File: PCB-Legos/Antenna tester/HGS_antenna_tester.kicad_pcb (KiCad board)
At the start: 4 copper layers, 100 x 100 mm, 10 parts, among them J1 Conn_Coaxial, J2 Conn_01x01

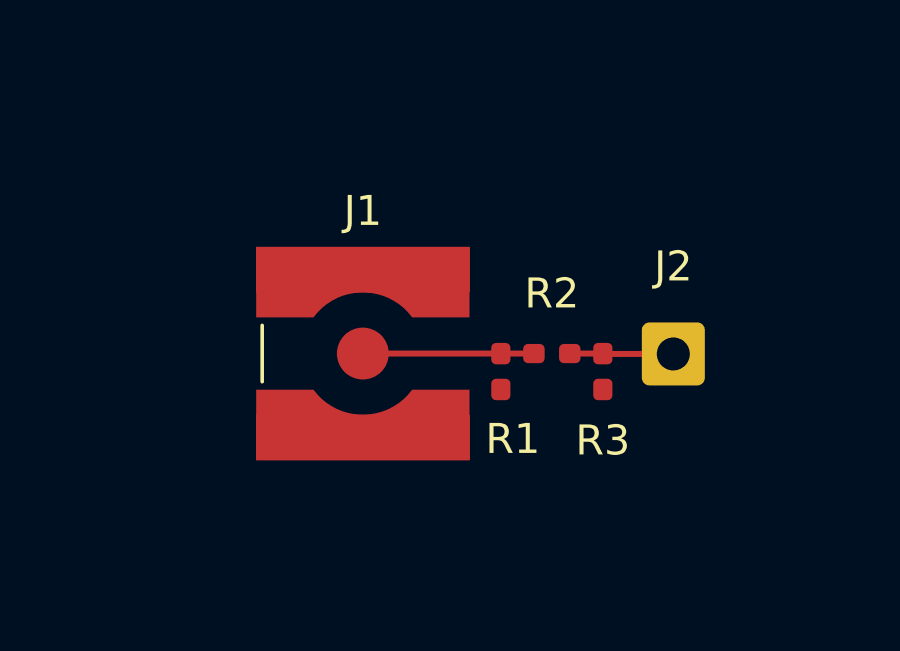
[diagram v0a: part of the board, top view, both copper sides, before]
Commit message: fixed microstrip width and moved SMA away from R1
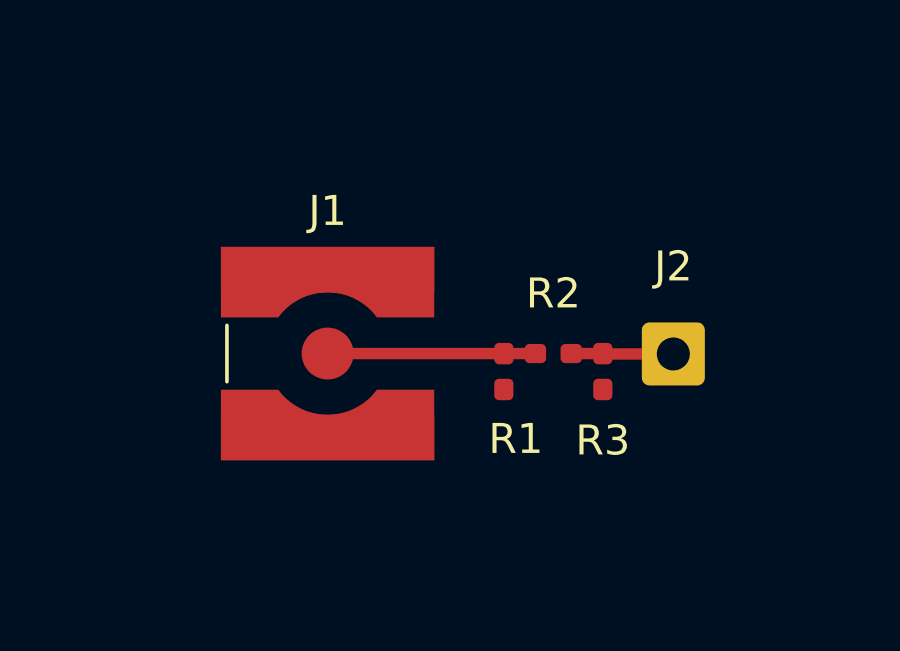
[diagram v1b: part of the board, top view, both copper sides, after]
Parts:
- moved J1 1.17 mm to (127.3, 85.0)
- moved R1 0.10 mm to (133.2, 85.6)
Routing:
- net Net-(J1-Pad1): track 5.71 -> 6.88 mm
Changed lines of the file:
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@@
     (pad "" np_thru_hole circle (at 0 0) (size 4.5 4.5) (drill 4.5) (layers *.Cu *.Mask))
   )
-  (footprint "Connector_Coaxial:SMA_Amphenol_132134-10_Vertical" locked (layer "F.Cu")
-    (at 128.5 85)
+  (footprint "Connector_Coaxial:SMA_Amphenol_132134-10_Vertical" (layer "F.Cu")
+    (at 127.325 85)
     (descr "https://www.amphenolrf.com/downloads/dl/file/id/4007/product/2974/132134_10_customer_drawing.pdf")
     (tags "SMA SMD Female Jack Vertical")
@@
     (pad "1" smd circle locked (at 0 0 90) (size 1.73 1.73) (layers "F.Cu" "F.Paste" "F.Mask")
       (net 2 "Net-(J1-Pad1)") (pinfunction "In") (pintype "passive"))
-    (pad "2" smd custom locked (at 0 2.8) (size 7.11 1.51) (layers "F.Cu" "F.Paste" "F.Mask")
+    (pad "2" smd custom (at 0 2.8) (size 7.11 1.51) (layers "F.Cu" "F.Paste" "F.Mask")
       (net 3 "GND") (pinfunction "Ext") (pintype "passive") (zone_connect 2)
       (options (clearance outline) (anchor rect))
@@
           ) (width 0) (fill yes))
       ))
-    (pad "2" smd custom locked (at 0 -2.8 180) (size 7.11 1.51) (layers "F.Cu" "F.Paste" "F.Mask")
+    (pad "2" smd custom (at 0 -2.8 180) (size 7.11 1.51) (layers "F.Cu" "F.Paste" "F.Mask")
       (net 3 "GND") (pinfunction "Ext") (pintype "passive") (zone_connect 2)
       (options (clearance outline) (anchor rect))
@@
   )
   (footprint "Resistor_SMD:R_0402_1005Metric_Pad0.72x0.64mm_HandSolder" (layer "F.Cu")
-    (at 134.8 85)
+    (at 134.85 85)
     (descr "Resistor SMD 0402 (1005 Metric), square (rectangular) end terminal, IPC_7351 nominal with elongated pad for handsoldering. (Body size source: IPC-SM-782 page 72, https://www.pcb-3d.com/wordpress/wp-content/uploads/ipc-sm-782a_amendment_1_and_2.pdf), generated with kicad-footprint-generator")
     (tags "resistor handsolder")
@@
   )
   (footprint "Resistor_SMD:R_0402_1005Metric_Pad0.72x0.64mm_HandSolder" (layer "F.Cu")
-    (at 133.1 85.6 -90)
+    (at 133.2 85.6 -90)
     (descr "Resistor SMD 0402 (1005 Metric), square (rectangular) end terminal, IPC_7351 nominal with elongated pad for handsoldering. (Body size source: IPC-SM-782 page 72, https://www.pcb-3d.com/wordpress/wp-content/uploads/ipc-sm-782a_amendment_1_and_2.pdf), generated with kicad-footprint-generator")
     (tags "resistor handsolder")
@@
   (segment (start 136.5 85.0025) (end 136.4975 85) (width 0.2) (layer "F.Cu") (net 1))
   (segment (start 136.511 85.0135) (end 136.5 85.0025) (width 0.2) (layer "F.Cu") (net 1))
-  (segment (start 138.8511 85.0135) (end 136.511 85.0135) (width 0.2) (layer "F.Cu") (net 1))
-  (segment (start 136.4975 85) (end 135.3975 85) (width 0.2) (layer "F.Cu") (net 1))
+  (segment (start 138.8511 85.0135) (end 136.511 85.0135) (width 0.38) (layer "F.Cu") (net 1))
+  (segment (start 136.4975 85) (end 135.3975 85) (width 0.38) (layer "F.Cu") (net 1))
   (segment (start 138.8401 85.0025) (end 138.8511 85.0135) (width 0.2) (layer "F.Cu") (net 1))
+  (segment (start 133.0975 85) (end 127.325 85) (width 0.38) (layer "F.Cu") (net 2))
   (segment (start 134.2 85.0025) (end 134.2025 85) (width 0.2) (layer "F.Cu") (net 2))
-  (segment (start 134.2025 85) (end 133.1025 85) (width 0.2) (layer "F.Cu") (net 2))
+  (segment (start 134.2025 85) (end 133.1025 85) (width 0.38) (layer "F.Cu") (net 2))
   (segment (start 133.1025 85) (end 133.1 85.0025) (width 0.2) (layer "F.Cu") (net 2))
   (segment (start 133.1 85.0025) (end 133.0975 85) (width 0.2) (layer "F.Cu") (net 2))
-  (segment (start 133.0975 85) (end 128.5 85) (width 0.2) (layer "F.Cu") (net 2))
   (zone (net 0) (net_name "") (layer "F.Cu") (hatch full 0.508)
     (connect_pads (clearance 0))

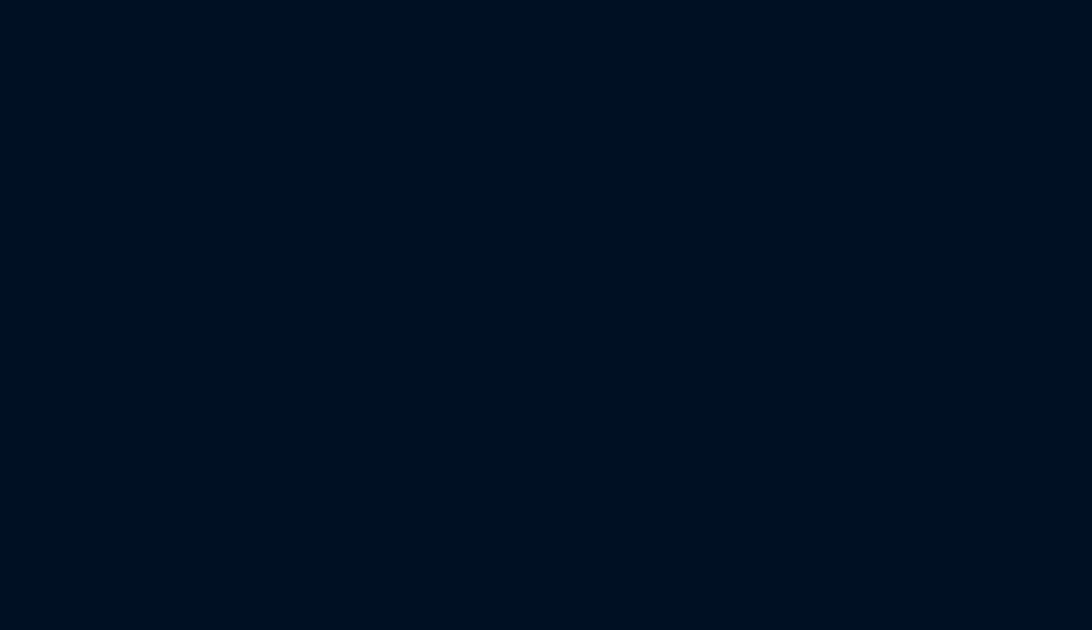
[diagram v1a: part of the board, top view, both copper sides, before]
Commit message: added missing antenna form mounting holes
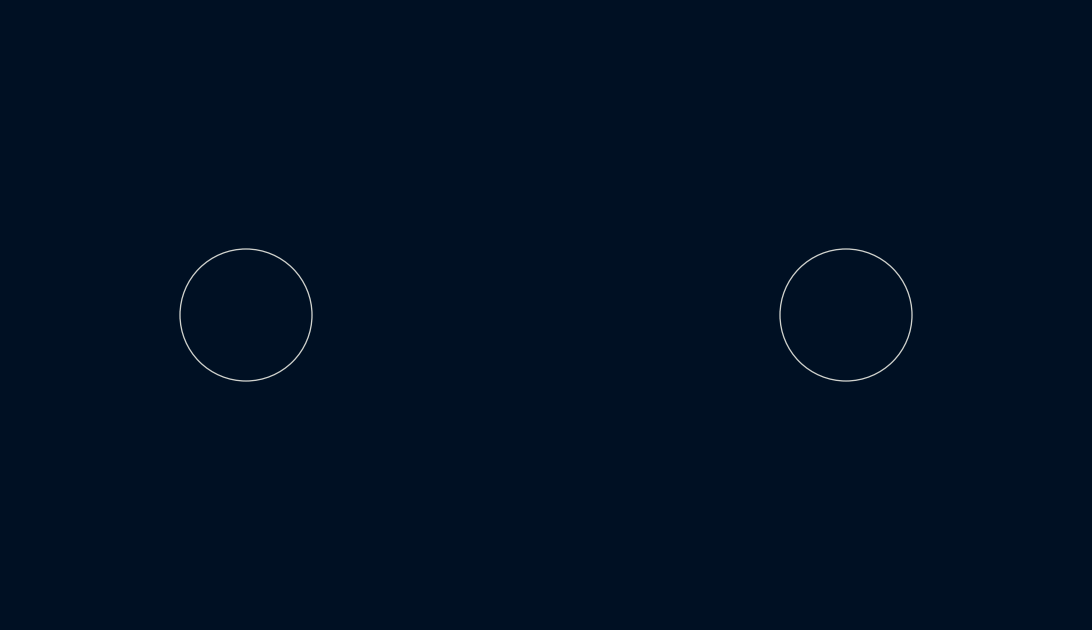
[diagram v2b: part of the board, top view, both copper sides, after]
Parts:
- added @HOLE4: , , F.Cu at (165.2, 129.8)
- added @HOLE5: , , F.Cu at (145.2, 129.8)
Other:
- board text added: "BLM18DN381SZ1D"
- board text added: "LP2985XX-N"
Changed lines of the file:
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@@
+  )
+  (footprint "" (layer "F.Cu")
+    (at 165.15 129.7535)
+    (fp_text reference "@HOLE4" (at 0 0) (layer "F.SilkS") hide
+      (effects (font (size 1.27 1.27) (thickness 0.15)))
+    )
+    (fp_text value "" (at 0 0) (layer "F.SilkS")
+      (effects (font (size 1.27 1.27) (thickness 0.15)))
+    )
+    (pad "" np_thru_hole circle (at 0 0) (size 4.4 4.4) (drill 4.4) (layers *.Cu *.Mask))
   )
   (footprint "" (layer "F.Cu")
@@
     )
     (pad "" np_thru_hole circle (at 0 0) (size 4.5 4.5) (drill 4.5) (layers *.Cu *.Mask))
+  )
+  (footprint "" (layer "F.Cu")
+    (at 145.15 129.7535)
+    (fp_text reference "@HOLE5" (at 0 0) (layer "F.SilkS") hide
+      (effects (font (size 1.27 1.27) (thickness 0.15)))
+    )
+    (fp_text value "" (at 0 0) (layer "F.SilkS")
+      (effects (font (size 1.27 1.27) (thickness 0.15)))
+    )
+    (pad "" np_thru_hole circle (at 0 0) (size 4.4 4.4) (drill 4.4) (layers *.Cu *.Mask))
   )
   (footprint "" (layer "F.Cu")
@@
   (gr_circle (center 155.1511 101.5135) (end 157.399 101.5135) (layer "Cmts.User") (width 0.001) (fill none))
   (gr_line (start 190.1511 106.5135) (end 177.1511 106.5135) (layer "Cmts.User") (width 0.001))
+  (gr_line (start 133.15 106.5135) (end 120.15 106.5135) (layer "Cmts.User") (width 0.001))
   (gr_line (start 187.1511 51.5135) (end 187.1511 61.5135) (layer "Cmts.User") (width 0.001))
   (gr_line (start 133.1511 106.5135) (end 120.1511 106.5135) (layer "Cmts.User") (width 0.001))
@@
   (gr_line (start 205.1511 150.5135) (end 205.1511 52.5135) (layer "Cmts.User") (width 0.001))
   (gr_arc (start 204.1511 51.5135) (mid 204.858207 51.806393) (end 205.1511 52.5135) (layer "Cmts.User") (width 0.001))
+  (gr_line (start 133.15 96.5135) (end 133.15 106.5135) (layer "Cmts.User") (width 0.001))
   (gr_arc (start 205.1511 150.5135) (mid 204.858207 151.220607) (end 204.1511 151.5135) (layer "Cmts.User") (width 0.001))
+  (gr_circle (center 145.149428 129.75816) (end 147.349428 129.75816) (layer "Cmts.User") (width 0.001) (fill none))
   (gr_line (start 177.1511 106.5135) (end 177.1511 96.5135) (layer "Cmts.User") (width 0.001))
+  (gr_circle (center 125.9 101.5135) (end 128.15 101.5135) (layer "Cmts.User") (width 0.001) (fill none))
   (gr_line (start 133.1511 96.5135) (end 133.1511 106.5135) (layer "Cmts.User") (width 0.001))
   (gr_line (start 133.1511 61.5135) (end 123.1511 61.5135) (layer "Cmts.User") (width 0.001))
   (gr_circle (center 125.9011 101.5135) (end 128.1511 101.5135) (layer "Cmts.User") (width 0.001) (fill none))
   (gr_arc (start 105.1511 52.5135) (mid 105.443993 51.806393) (end 106.1511 51.5135) (layer "Cmts.User") (width 0.001))
+  (gr_line (start 120.15 96.5135) (end 133.15 96.5135) (layer "Cmts.User") (width 0.001))
   (gr_line (start 155.1511 96.47251) (end 152.96829 97.73276) (layer "Cmts.User") (width 0.001))
   (gr_line (start 123.1511 61.5135) (end 123.1511 51.5135) (layer "Cmts.User") (width 0.001))
@@
   (gr_line (start 105.1511 52.5135) (end 105.1511 150.5135) (layer "Cmts.User") (width 0.001))
   (gr_circle (center 184.4011 101.5135) (end 186.6511 101.5135) (layer "Cmts.User") (width 0.001) (fill none))
+  (gr_circle (center 165.149428 129.75816) (end 167.349428 129.75816) (layer "Cmts.User") (width 0.001) (fill none))
   (gr_line (start 152.96829 97.73276) (end 150.785468 98.993) (layer "Cmts.User") (width 0.001))
   (gr_circle (center 182.1511 56.5135) (end 184.3511 56.5135) (layer "Cmts.User") (width 0.001) (fill none))
@@
     (effects (font (size 1.63576 1.63576) (thickness 0.14224)) (justify left bottom))
   )
+  (gr_text "LP2985XX-N" (at 311.575 102.525) (layer "F.Fab")
+    (effects (font (size 0.7456 0.7456) (thickness 0.0544)) (justify left))
+  )
+  (gr_text "BLM18DN381SZ1D" (at 305.875 123.825) (layer "F.Fab")
+    (effects (font (size 0.7456 0.7456) (thickness 0.0544)) (justify left))
+  )
   (segment (start 136.5 85.0025) (end 136.4975 85) (width 0.2) (layer "F.Cu") (net 1))
